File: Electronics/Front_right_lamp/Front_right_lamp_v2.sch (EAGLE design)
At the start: 9 parts, among them X1 B4B-ZR

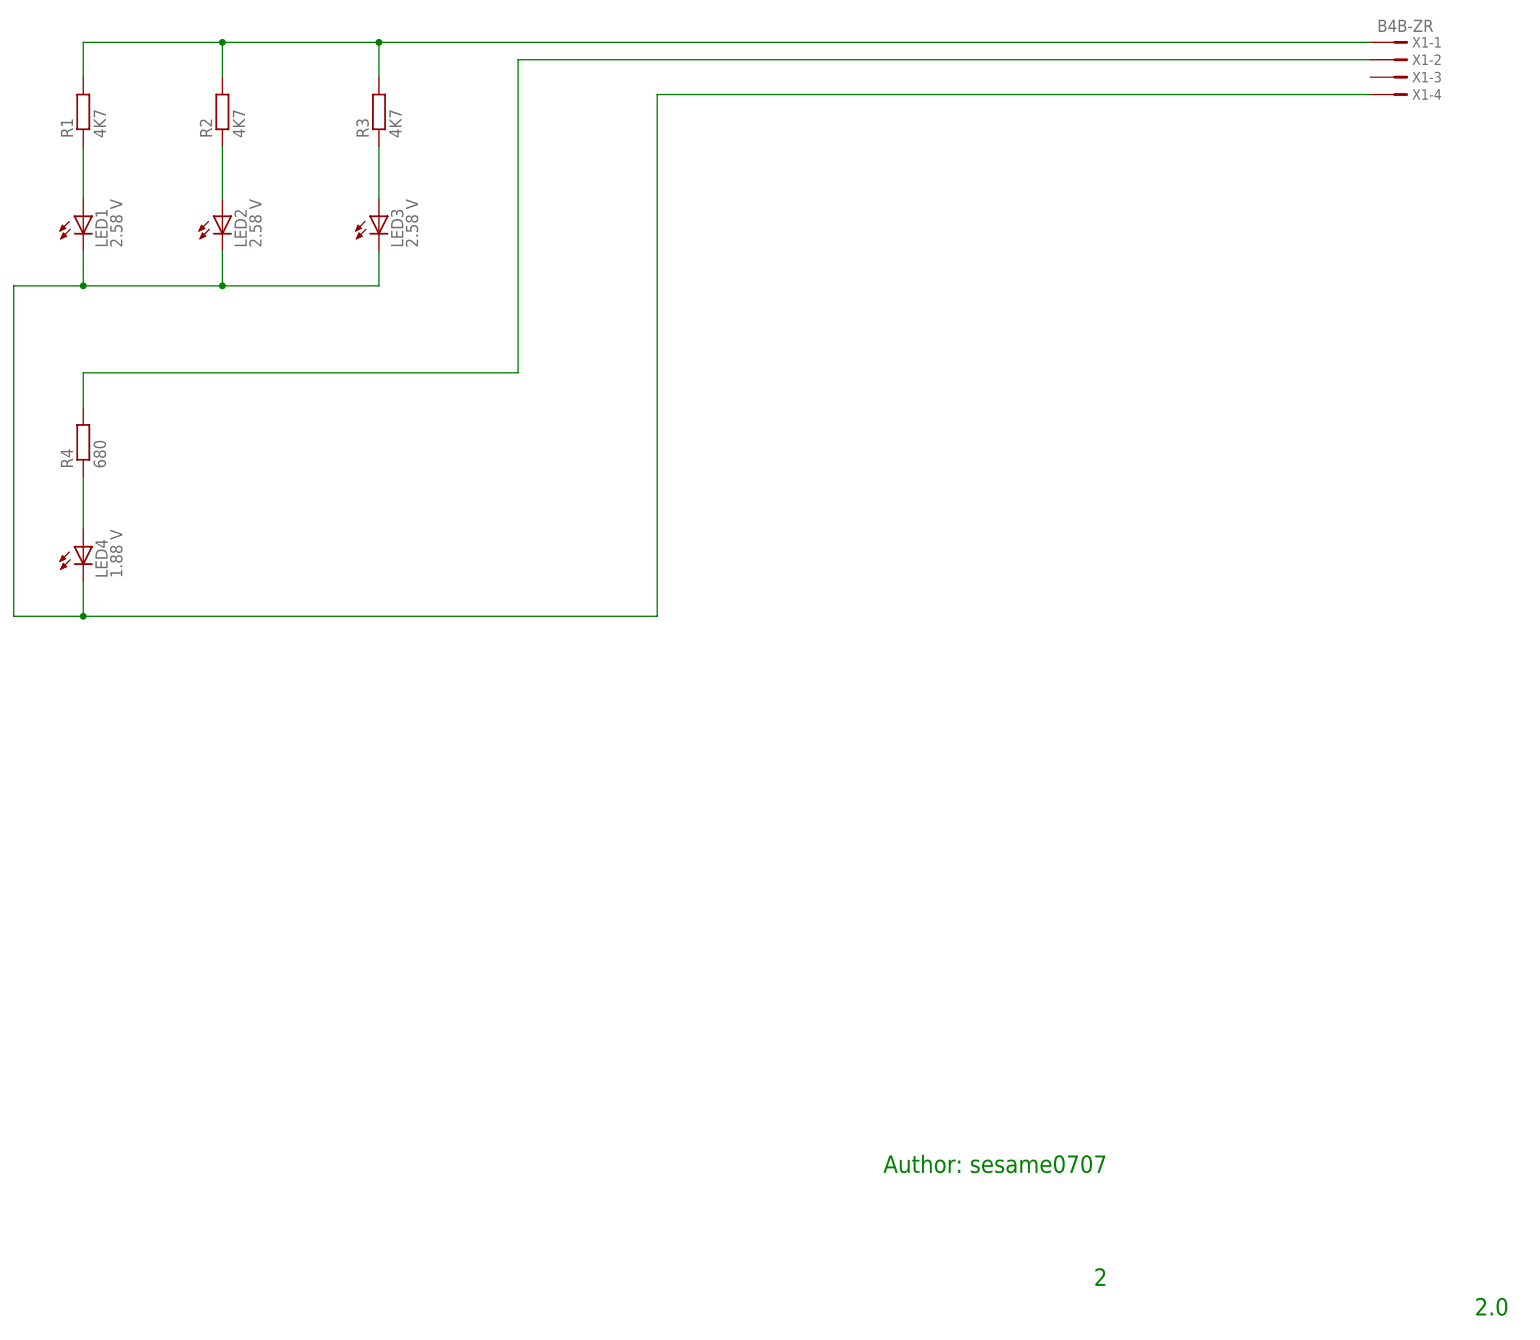
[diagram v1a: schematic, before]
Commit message: Front and rear lamps done
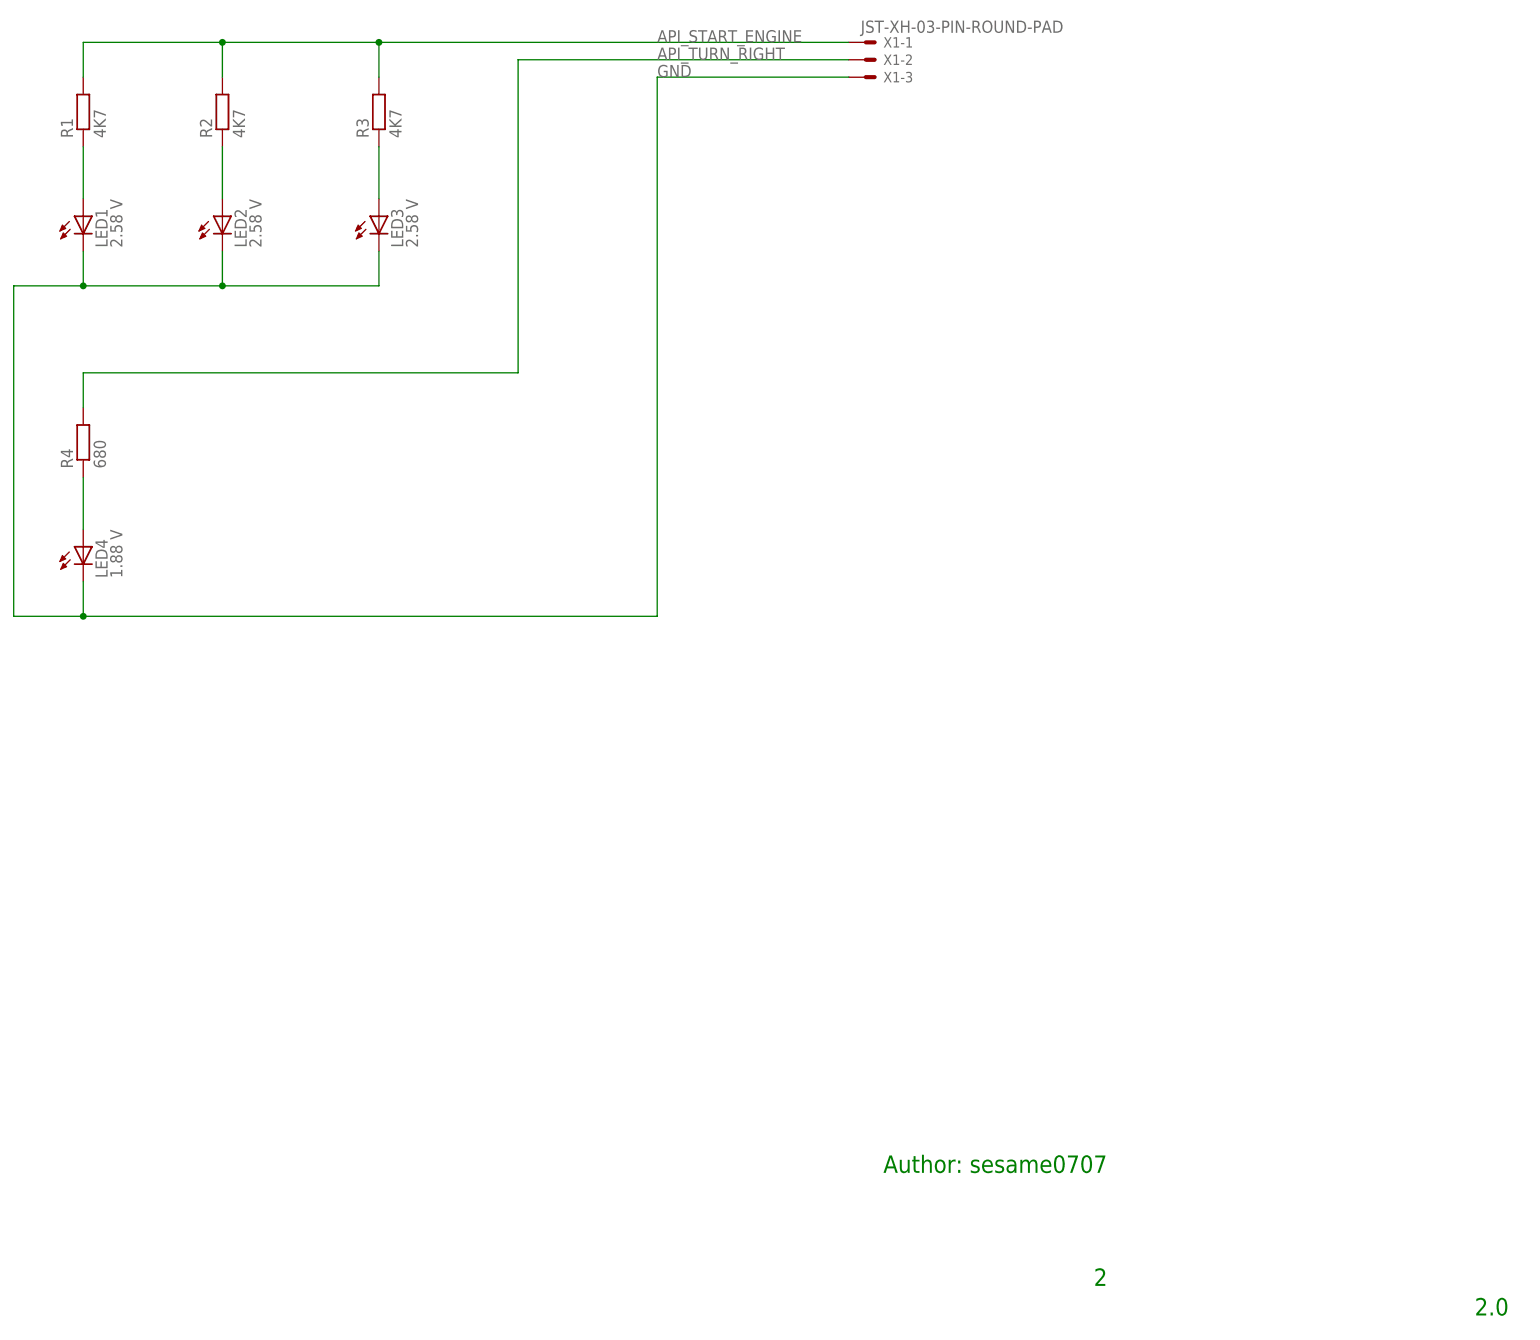
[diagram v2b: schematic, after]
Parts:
- LED1, LED2, LED3: COLOR (none) -> White
- LED4: COLOR (none) -> Yellow
- X1: value B4B-ZR -> JST-XH-03-PIN-ROUND-PAD; device con-jst:B4B-ZR -> Rembrandt Electronics - JST XH Connectors v1-0:JST-XH-03-PIN-ROUND-PAD
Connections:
- removed net N$5: R1.2, R2.2, R3.2, X1-1.1
- removed net N$6: R4.2, X1-2.1
- removed net N$7: LED1.C, LED2.C, LED3.C, LED4.C, X1-4.1
- new net API_START_ENGINE: R1.2, R2.2, R3.2, X1-1.S
- new net API_TURN_RIGHT: R4.2, X1-2.S
- new net GND: LED1.C, LED2.C, LED3.C, LED4.C, X1-3.S
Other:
- moved on the sheet: X1-1, X1-2, X1-3
